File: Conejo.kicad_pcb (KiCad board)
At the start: 4 copper layers, 130.3 x 112.5 mm, 117 parts, among them J1 BATT, J2 HRO_TYPE-C-31-M-12, J3 JTAG_TC2030, J4 RGB, Q1 2N7002, Q2 2N7002, Q3 AO3407, SW1 PWR, SW10 MX Hotswap, SW11 MX Hotswap, SW12 MX Hotswap, SW13 MX Hotswap, SW14 MX Hotswap, SW15 MX Hotswap, SW16 MX Hotswap, SW17 MX Hotswap, SW18 MX Hotswap, SW19 MX Hotswap, SW2 MX Hotswap, SW20 MX Hotswap, SW21 MX Hotswap, SW22 MX Hotswap, SW23 MX Hotswap, SW24 MX Hotswap, SW25 MX Hotswap, SW26 MX Hotswap, SW27 MX Hotswap, SW28 MX Hotswap, SW29 RESET, SW3 MX Hotswap, SW4 MX Hotswap, SW5 MX Hotswap, SW6 MX Hotswap, SW7 MX Hotswap, SW8 MX Hotswap, SW9 MX Hotswap, U1 BQ24075RGT, U2 MAX17048, U3 SRV05-4, U4 MS88SF3

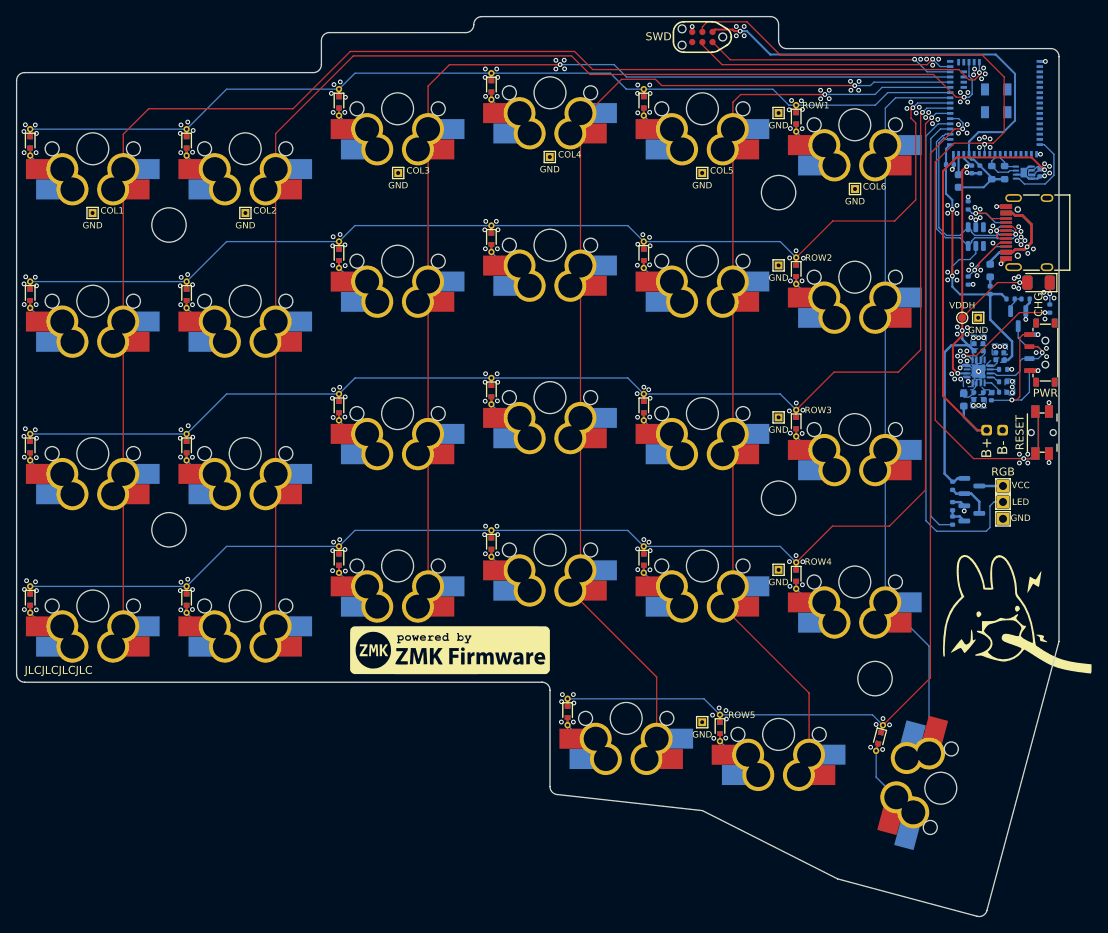
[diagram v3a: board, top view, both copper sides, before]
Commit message: feat(pcb): Switch from 4.3mm NPTH mounting holes to M2 PTH
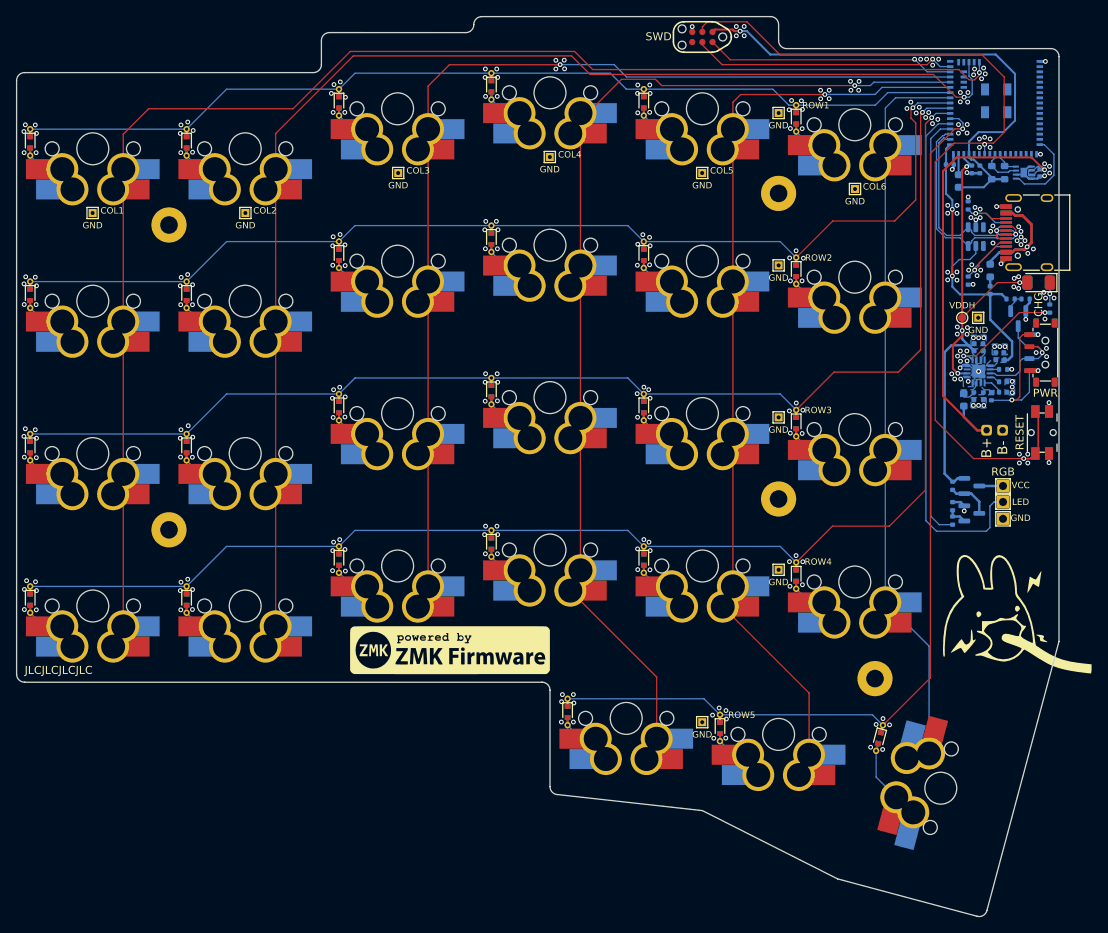
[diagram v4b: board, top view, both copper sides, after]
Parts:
- H1, H2, H3, H4, H5: value 4.3mm -> M2; footprint Conejo:MountingHole_4.3mm -> MountingHole:MountingHole_2.2mm_M2_Pad
- moved H4 0.10 mm to (85.7, 45.8)
- moved H2 0.10 mm to (85.7, 7.58)
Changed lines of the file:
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@@
   (net 108 "unconnected-(U3-Pad3)")
   (net 109 "unconnected-(U3-Pad4)")
-  (footprint "Conejo:MountingHole_4.3mm" (layer "F.Cu")
-    (at 85.725 45.675)
-    (descr "Mounting Hole 4.3mm, no annular, M4")
-    (tags "mounting hole 4.3mm no annular m4")
+  (footprint "MountingHole:MountingHole_2.2mm_M2_Pad" (layer "F.Cu")
+    (at 85.725 45.775)
+    (descr "Mounting Hole 2.2mm, M2")
+    (tags "mounting hole 2.2mm m2")
     (property "Sheetfile" "nRF52840.kicad_sch")
     (property "Sheetname" "nRF52840 Module")
     (attr exclude_from_pos_files)
-    (fp_text reference "H4" (at 0 -5.3) (layer "F.SilkS") hide
+    (fp_text reference "H4" (at 0 -3.2) (layer "F.SilkS") hide
       (effects (font (size 1 1) (thickness 0.15)))
     )
-    (fp_text value "4.3mm" (at 0 5.3) (layer "F.Fab")
+    (fp_text value "M2" (at 0 3.2) (layer "F.Fab")
       (effects (font (size 1 1) (thickness 0.15)))
     )
@@
       (effects (font (size 1 1) (thickness 0.15)))
     )
-    (pad "" np_thru_hole circle (at 0 0) (size 4.3 4.3) (drill 4.3) (layers F&B.Cu *.Mask))
+    (fp_circle (center 0 0) (end 2.2 0) (layer "Cmts.User") (width 0.15) (fill none))
+    (fp_circle (center 0 0) (end 2.45 0) (layer "F.CrtYd") (width 0.05) (fill none))
+    (pad "1" thru_hole circle (at 0 0) (size 4.4 4.4) (drill 2.2) (layers *.Cu *.Mask)
+      (net 2 "GND") (pinfunction "1") (pintype "input"))
   )
   (footprint "Conejo:D_SOD-523 (Reversible)" (layer "F.Cu")
@@
       (net 2 "GND") (pinfunction "1") (pintype "passive"))
   )
-  (footprint "Conejo:MountingHole_4.3mm" (layer "F.Cu")
+  (footprint "MountingHole:MountingHole_2.2mm_M2_Pad" (layer "F.Cu")
     (at 9.525 49.625)
-    (descr "Mounting Hole 4.3mm, no annular, M4")
-    (tags "mounting hole 4.3mm no annular m4")
+    (descr "Mounting Hole 2.2mm, M2")
+    (tags "mounting hole 2.2mm m2")
     (property "Sheetfile" "nRF52840.kicad_sch")
     (property "Sheetname" "nRF52840 Module")
     (attr exclude_from_pos_files)
-    (fp_text reference "H3" (at 0 -5.3) (layer "F.SilkS") hide
+    (fp_text reference "H3" (at 0 -3.2) (layer "F.SilkS") hide
       (effects (font (size 1 1) (thickness 0.15)))
     )
-    (fp_text value "4.3mm" (at 0 5.3) (layer "F.Fab")
+    (fp_text value "M2" (at 0 3.2) (layer "F.Fab")
       (effects (font (size 1 1) (thickness 0.15)))
     )
@@
       (effects (font (size 1 1) (thickness 0.15)))
     )
-    (pad "" np_thru_hole circle (at 0 0) (size 4.3 4.3) (drill 4.3) (layers F&B.Cu *.Mask))
+    (fp_circle (center 0 0) (end 2.2 0) (layer "Cmts.User") (width 0.15) (fill none))
+    (fp_circle (center 0 0) (end 2.45 0) (layer "F.CrtYd") (width 0.05) (fill none))
+    (pad "1" thru_hole circle (at 0 0) (size 4.4 4.4) (drill 2.2) (layers *.Cu *.Mask)
+      (net 2 "GND") (pinfunction "1") (pintype "input"))
   )
   (footprint "Conejo:D_SOD-523 (Reversible)" (layer "F.Cu")
@@
     )
   )
-  (footprint "Conejo:MountingHole_4.3mm" (layer "F.Cu")
+  (footprint "MountingHole:MountingHole_2.2mm_M2_Pad" (layer "F.Cu")
     (at 97.775 68.225 90)
-    (descr "Mounting Hole 4.3mm, no annular, M4")
-    (tags "mounting hole 4.3mm no annular m4")
+    (descr "Mounting Hole 2.2mm, M2")
+    (tags "mounting hole 2.2mm m2")
     (property "Sheetfile" "nRF52840.kicad_sch")
     (property "Sheetname" "nRF52840 Module")
     (attr exclude_from_pos_files)
-    (fp_text reference "H5" (at 0 -5.3 90) (layer "F.SilkS") hide
+    (fp_text reference "H5" (at 0 -3.2 90) (layer "F.SilkS") hide
       (effects (font (size 1 1) (thickness 0.15)))
     )
-    (fp_text value "4.3mm" (at 0 5.3 90) (layer "F.Fab")
+    (fp_text value "M2" (at 0 3.2 90) (layer "F.Fab")
       (effects (font (size 1 1) (thickness 0.15)))
     )
@@
       (effects (font (size 1 1) (thickness 0.15)))
     )
-    (pad "" np_thru_hole circle (at 0 0 90) (size 4.3 4.3) (drill 4.3) (layers F&B.Cu *.Mask))
+    (fp_circle (center 0 0) (end 2.2 0) (layer "Cmts.User") (width 0.15) (fill none))
+    (fp_circle (center 0 0) (end 2.45 0) (layer "F.CrtYd") (width 0.05) (fill none))
+    (pad "1" thru_hole circle (at 0 0 90) (size 4.4 4.4) (drill 2.2) (layers *.Cu *.Mask)
+      (net 2 "GND") (pinfunction "1") (pintype "input"))
   )
   (footprint "Conejo:D_SOD-523 (Reversible)" (layer "F.Cu")
@@
       (net 2 "GND") (pinfunction "1") (pintype "passive"))
   )
-  (footprint "Conejo:MountingHole_4.3mm" (layer "F.Cu")
+  (footprint "MountingHole:MountingHole_2.2mm_M2_Pad" (layer "F.Cu")
     (at 9.525 11.525)
-    (descr "Mounting Hole 4.3mm, no annular, M4")
-    (tags "mounting hole 4.3mm no annular m4")
+    (descr "Mounting Hole 2.2mm, M2")
+    (tags "mounting hole 2.2mm m2")
     (property "Sheetfile" "nRF52840.kicad_sch")
     (property "Sheetname" "nRF52840 Module")
     (attr exclude_from_pos_files)
-    (fp_text reference "H1" (at 0 -5.3) (layer "F.SilkS") hide
+    (fp_text reference "H1" (at 0 -3.2) (layer "F.SilkS") hide
       (effects (font (size 1 1) (thickness 0.15)))
     )
-    (fp_text value "4.3mm" (at 0 5.3) (layer "F.Fab")
+    (fp_text value "M2" (at 0 3.2) (layer "F.Fab")
       (effects (font (size 1 1) (thickness 0.15)))
     )
@@
       (effects (font (size 1 1) (thickness 0.15)))
     )
-    (pad "" np_thru_hole circle (at 0 0) (size 4.3 4.3) (drill 4.3) (layers F&B.Cu *.Mask))
+    (fp_circle (center 0 0) (end 2.2 0) (layer "Cmts.User") (width 0.15) (fill none))
+    (fp_circle (center 0 0) (end 2.45 0) (layer "F.CrtYd") (width 0.05) (fill none))
+    (pad "1" thru_hole circle (at 0 0) (size 4.4 4.4) (drill 2.2) (layers *.Cu *.Mask)
+      (net 2 "GND") (pinfunction "1") (pintype "input"))
   )
   (footprint "Conejo:USB_C_Receptacle_HRO_TYPE-C-31-M-12 (Reversible)" (layer "F.Cu")
@@
       (net 19 "Net-(D13-Pad2)") (pinfunction "2") (pintype "passive"))
   )
-  (footprint "Conejo:MountingHole_4.3mm" (layer "F.Cu")
-    (at 85.725 7.475)
-    (descr "Mounting Hole 4.3mm, no annular, M4")
-    (tags "mounting hole 4.3mm no annular m4")
+  (footprint "MountingHole:MountingHole_2.2mm_M2_Pad" (layer "F.Cu")
+    (at 85.725 7.575)
+    (descr "Mounting Hole 2.2mm, M2")
+    (tags "mounting hole 2.2mm m2")
     (property "Sheetfile" "nRF52840.kicad_sch")
     (property "Sheetname" "nRF52840 Module")
     (attr exclude_from_pos_files)
-    (fp_text reference "H2" (at 0 -5.3) (layer "F.SilkS") hide
+    (fp_text reference "H2" (at 0 -3.2) (layer "F.SilkS") hide
       (effects (font (size 1 1) (thickness 0.15)))
     )
-    (fp_text value "4.3mm" (at 0 5.3) (layer "F.Fab")
+    (fp_text value "M2" (at 0 3.2) (layer "F.Fab")
       (effects (font (size 1 1) (thickness 0.15)))
     )
@@
       (effects (font (size 1 1) (thickness 0.15)))
     )
-    (pad "" np_thru_hole circle (at 0 0) (size 4.3 4.3) (drill 4.3) (layers F&B.Cu *.Mask))
+    (fp_circle (center 0 0) (end 2.2 0) (layer "Cmts.User") (width 0.15) (fill none))
+    (fp_circle (center 0 0) (end 2.45 0) (layer "F.CrtYd") (width 0.05) (fill none))
+    (pad "1" thru_hole circle (at 0 0) (size 4.4 4.4) (drill 2.2) (layers *.Cu *.Mask)
+      (net 2 "GND") (pinfunction "1") (pintype "input"))
   )
   (footprint "Conejo:D_SOD-523 (Reversible)" (layer "F.Cu")

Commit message: feat(3D): Re-export model with M3 holes with vias
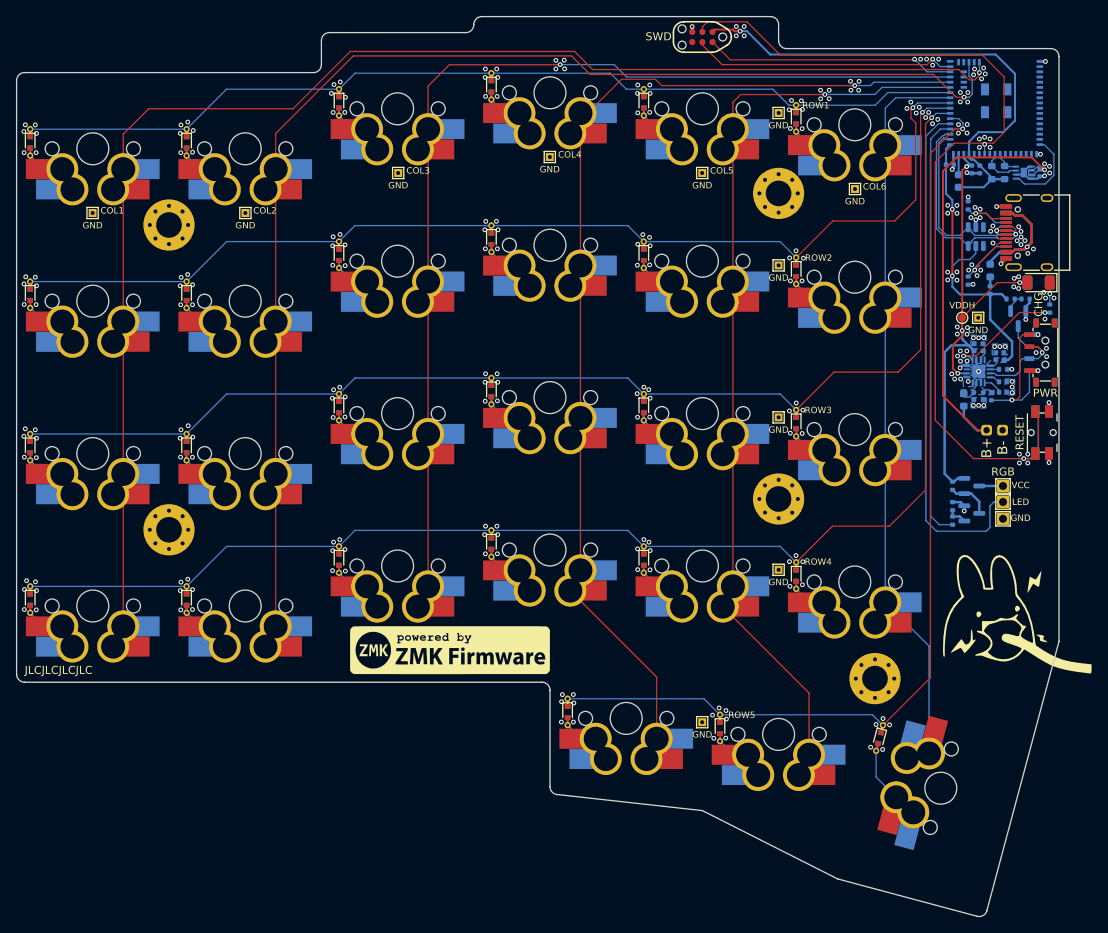
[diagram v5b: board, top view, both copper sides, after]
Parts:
- H1, H2, H3, H4, H5: value M2 -> M3; footprint MountingHole:MountingHole_2.2mm_M2_Pad -> MountingHole:MountingHole_3.2mm_M3_Pad_Via
- turned H5 to 0 degrees
